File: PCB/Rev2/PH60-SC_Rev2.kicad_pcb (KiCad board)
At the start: 2 copper layers, 285 x 94.6 mm, 236 parts, among them J1 USB_C_Receptacle_USB2.0_14P, J2 Conn_01x02_Pin, J3 Conn_01x02_Pin, Q1 2N7002, Q2 BSS84, U1 nRF52840, U2 ETA6093, X1 32.768kHz, X2 Crystal_Generic

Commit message: drc
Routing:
- net ADC: track 54.0 -> 55.7 mm
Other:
- board text added: "G"
- board text added: "PH60 Slim-Choc V2"
- board text added: "R"

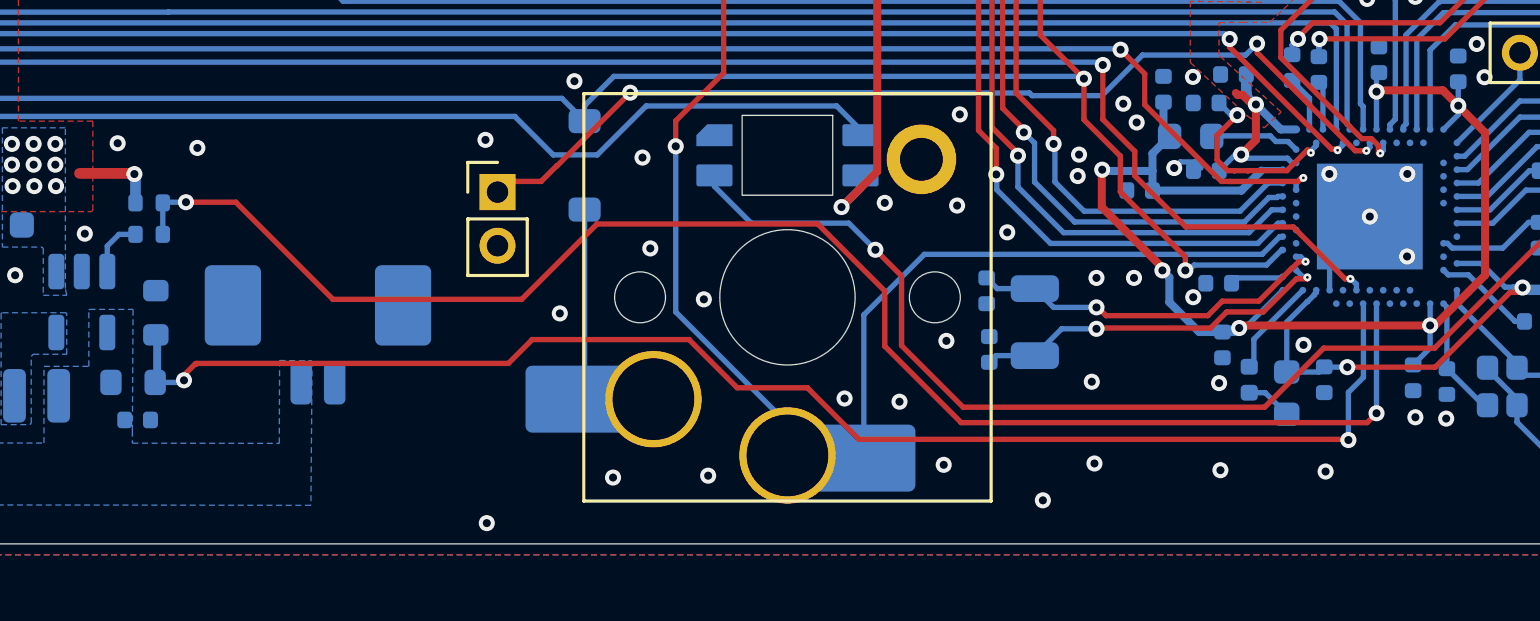
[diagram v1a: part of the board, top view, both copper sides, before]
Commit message: Change boot pin location
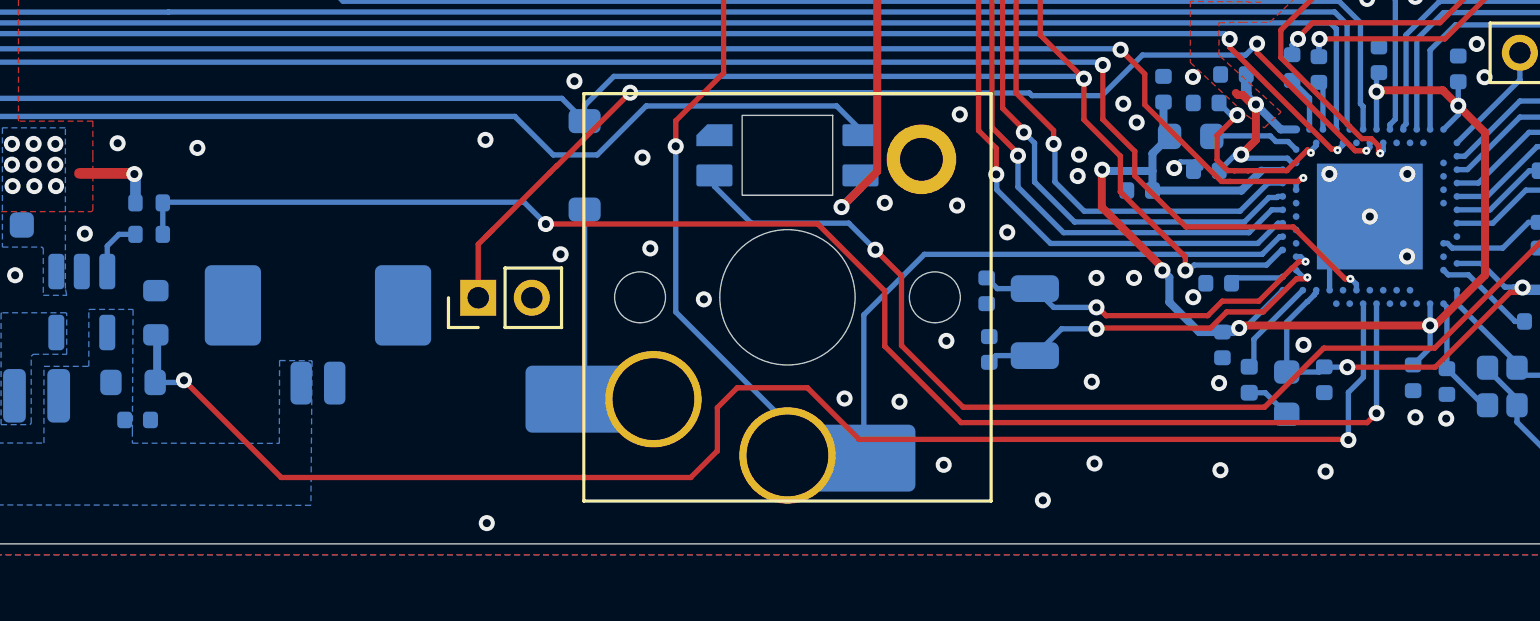
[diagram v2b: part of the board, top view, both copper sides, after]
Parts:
- moved J3 4.01 mm to (148.0, 114.3), turned to 90 degrees
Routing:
- net /RESET: track 36.5 -> 40.9 mm
- net CHRG: track 57.6 -> 55.3 mm
- net ADC: track 55.7 -> 58.0 mm
- net GND: vias 478 -> 476
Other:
- board text added: "BOOT"
- board text removed: "G"
- board text removed: "R"
